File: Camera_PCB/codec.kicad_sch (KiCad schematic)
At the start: 8 parts

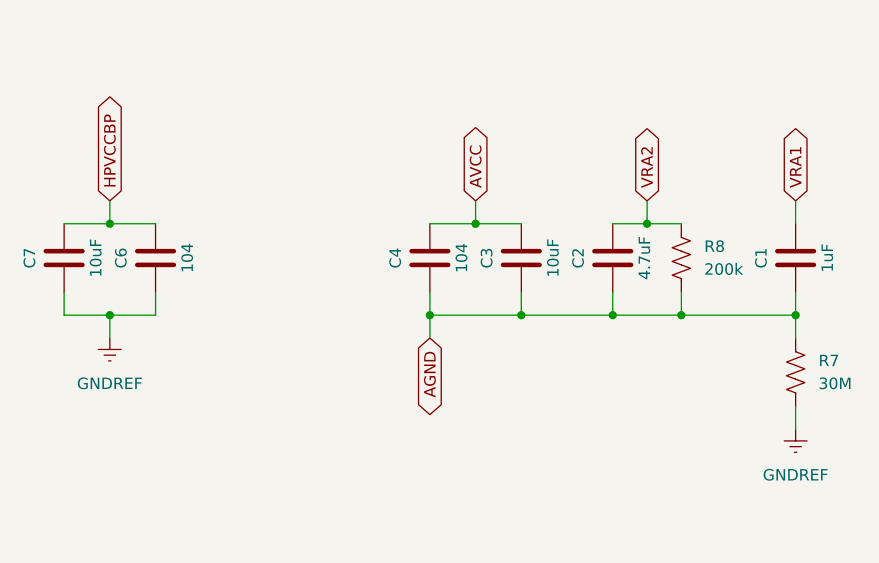
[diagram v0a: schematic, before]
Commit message: Fixed Capacitor Naming
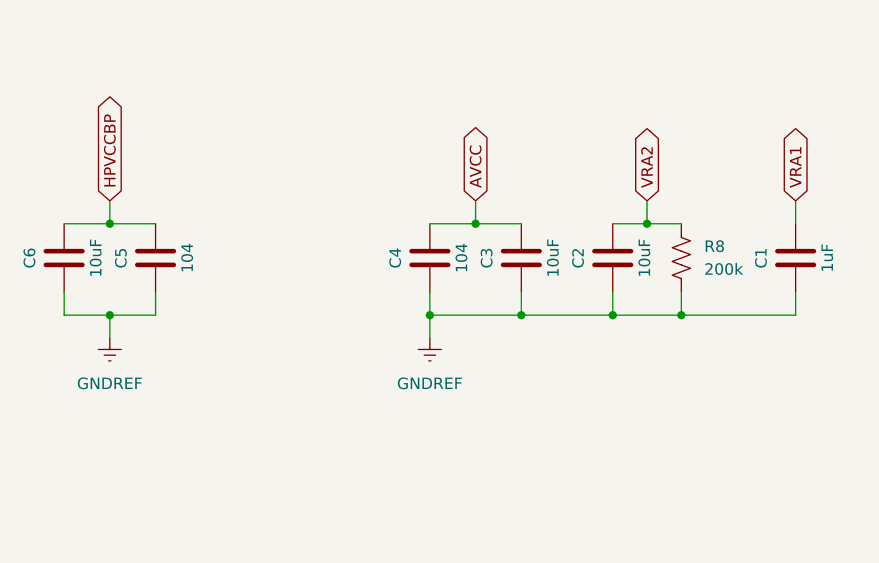
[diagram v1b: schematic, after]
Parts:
- removed R7: 30M, symbol Device:R_US
- C2: value 4.7uF -> 10uF
- renumbered C6 to C5, C7 to C6
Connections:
- net AGND is gone; now on net GNDREF: C1.1, C2.1, C3.1, C4.1, R8.2
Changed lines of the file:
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@@
-	)
-	(junction
-		(at 187.96 110.49)
-		(diameter 0)
-		(color 0 0 0 0)
 	)
 	(junction
@@
 	(wire
 		(pts
-			(xy 187.96 110.49) (xy 187.96 113.03)
-		)
-		(stroke
-			(width 0)
-			(type default)
-		)
-	)
-	(wire
-		(pts
 			(xy 175.26 107.95) (xy 175.26 110.49)
 		)
@@
 	(wire
 		(pts
-			(xy 187.96 120.65) (xy 187.96 123.19)
-		)
-		(stroke
-			(width 0)
-			(type default)
-		)
-	)
-	(wire
-		(pts
 			(xy 157.48 110.49) (xy 167.64 110.49)
 		)
@@
 			(width 0)
 			(type default)
-		)
-	)
-	(global_label "AGND"
-		(shape bidirectional)
-		(at 147.32 113.03 270)
-		(fields_autoplaced yes)
-		(effects
-			(font
-				(size 1.27 1.27)
-			)
-			(justify right)
-		)
-		(property "Intersheetrefs" "${INTERSHEET_REFS}"
-			(at 147.32 122.0856 90)
-			(effects
-				(font
-					(size 1.27 1.27)
-				)
-				(justify right)
-				(hide yes)
-			)
 		)
 	)
@@
 		(on_board yes)
 		(dnp no)
-		(property "Reference" "C6"
+		(property "Reference" "C5"
 			(at 113.03 104.14 90)
 			(effects
@@
 			(project "Camera_PCB"
 				(path "/400c1603-202c-4359-a830-d2f0d06dd3ce/6e10c56a-e5a3-4901-929f-3bc6ae5eaa96"
-					(reference "C6")
+					(reference "C5")
 					(unit 1)
 				)
@@
 			)
 		)
-		(property "Value" "4.7uF"
+		(property "Value" "10uF"
 			(at 171.196 104.14 90)
 			(effects
@@
 		(on_board yes)
 		(dnp no)
-		(property "Reference" "C7"
+		(property "Reference" "C6"
 			(at 102.87 104.14 90)
 			(effects
@@
 			(project "Camera_PCB"
 				(path "/400c1603-202c-4359-a830-d2f0d06dd3ce/6e10c56a-e5a3-4901-929f-3bc6ae5eaa96"
-					(reference "C7")
+					(reference "C6")
 					(unit 1)
 				)
@@
 	)
 	(symbol
-		(lib_id "Device:R_US")
-		(at 187.96 116.84 0)
-		(unit 1)
-		(exclude_from_sim no)
-		(in_bom yes)
-		(on_board yes)
-		(dnp no)
-		(fields_autoplaced yes)
-		(property "Reference" "R7"
-			(at 190.5 115.5699 0)
-			(effects
-				(font
-					(size 1.27 1.27)
-				)
-				(justify left)
-			)
-		)
-		(property "Value" "30M"
-			(at 190.5 118.1099 0)
-			(effects
-				(font
-					(size 1.27 1.27)
-				)
-				(justify left)
-			)
-		)
-		(property "Footprint" ""
-			(at 188.976 117.094 90)
-			(effects
-				(font
-					(size 1.27 1.27)
-				)
-				(hide yes)
-			)
-		)
-		(property "Datasheet" "~"
-			(at 187.96 116.84 0)
-			(effects
-				(font
-					(size 1.27 1.27)
-				)
-				(hide yes)
-			)
-		)
-		(property "Description" "Resistor, US symbol"
-			(at 187.96 116.84 0)
-			(effects
-				(font
-					(size 1.27 1.27)
-				)
-				(hide yes)
-			)
-		)
-		(pin "1"
-		)
-		(pin "2"
-		)
-		(instances
-			(project "Camera_PCB"
-				(path "/400c1603-202c-4359-a830-d2f0d06dd3ce/6e10c56a-e5a3-4901-929f-3bc6ae5eaa96"
-					(reference "R7")
-					(unit 1)
-				)
-			)
-		)
-	)
-	(symbol
 		(lib_id "power:GNDREF")
-		(at 187.96 123.19 0)
+		(at 147.32 113.03 0)
 		(unit 1)
 		(exclude_from_sim no)
@@
 		(fields_autoplaced yes)
 		(property "Reference" "#PWR011"
-			(at 187.96 129.54 0)
+			(at 147.32 119.38 0)
 			(effects
 				(font
@@
 		)
 		(property "Value" "GNDREF"
-			(at 187.96 128.27 0)
+			(at 147.32 118.11 0)
 			(effects
 				(font
@@
 		)
 		(property "Footprint" ""
-			(at 187.96 123.19 0)
+			(at 147.32 113.03 0)
 			(effects
 				(font
@@
 		)
 		(property "Datasheet" ""
-			(at 187.96 123.19 0)
+			(at 147.32 113.03 0)
 			(effects
 				(font
@@
 		)
 		(property "Description" "Power symbol creates a global label with name \"GNDREF\" , reference supply ground"
-			(at 187.96 123.19 0)
-			(effects
-				(font
+			(at 147.32 113.03 0)
+			(effects
+				(font

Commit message: Camera connections added
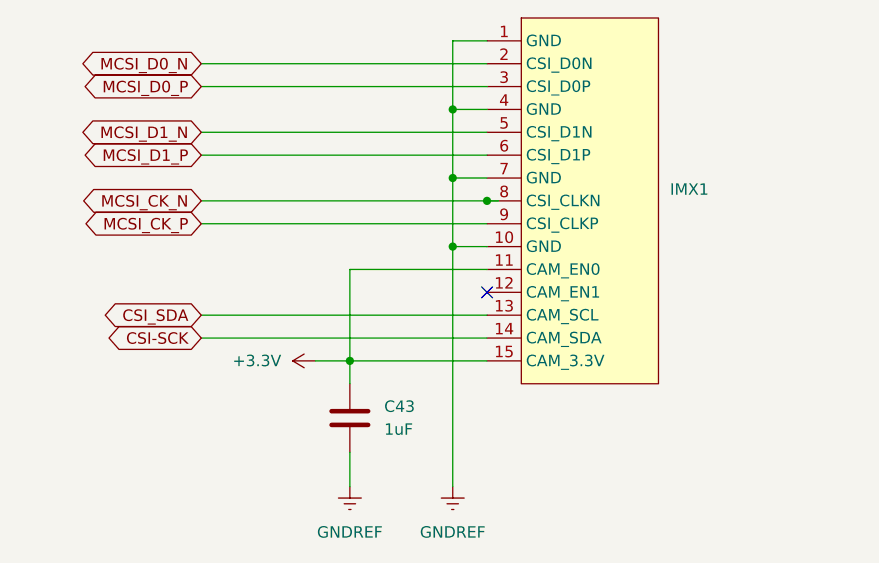
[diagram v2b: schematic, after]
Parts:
- removed C1: 1uF, symbol Device:C
- removed C2, C3, C6: 10uF, symbol Device:C
- removed C4, C5: 104, symbol Device:C
- removed R8: 200k, symbol Device:R_US
- added C43: 1uF, symbol Device:C
- added IMX1: ~, symbol custom_chips:IMX219_Camera
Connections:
- net GNDREF: now also C43.2, IMX1.1 (GND), IMX1.10 (GND), IMX1.4 (GND), IMX1.7 (GND)
- new net +3.3V: C43.1, IMX1.11 (CAM_EN0), IMX1.15 (CAM_3.3V)
- new net CSI-SCK: IMX1.14 (CAM_SDA)
- new net CSI_SDA: IMX1.13 (CAM_SCL)
- new net MCSI_CK_N: IMX1.8 (CSI_CLKN)
- new net MCSI_CK_P: IMX1.9 (CSI_CLKP)
- new net MCSI_D0_N: IMX1.2 (CSI_D0N)
- new net MCSI_D0_P: IMX1.3 (CSI_D0P)
- new net MCSI_D1_N: IMX1.5 (CSI_D1N)
- new net MCSI_D1_P: IMX1.6 (CSI_D1P)
- no-connect marks 0 -> 1
